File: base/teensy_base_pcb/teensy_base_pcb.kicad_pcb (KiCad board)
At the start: 2 copper layers, 69.8 x 48.3 mm, 26 parts, among them Q1 PN2222A, U1 LM7805CT, U2 LD1117V33, U3 Teensy_3.2, U4 nRF24L01+

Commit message: PCB updates / clean up.
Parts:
- removed R3: 10K, Resistors_ThroughHole:Resistor_Horizontal_RM10mm
- removed R4: 270, Resistors_ThroughHole:Resistor_Horizontal_RM10mm
- added R1: 10K, Resistors_ThroughHole:Resistor_Horizontal_RM10mm, F.Cu at (213.9, 104.1)
- added R2: 270, Resistors_ThroughHole:Resistor_Horizontal_RM10mm, F.Cu at (176.5, 101.6)
- moved U4 7.71 mm to (211.8, 87.4), turned to 180 degrees
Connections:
- U3 pad 21: Net-(P_SERVO1-Pad1) -> NC
- U3 pad 3: NC -> Net-(P_SERVO1-Pad1)
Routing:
- net Net-(P_SERVO1-Pad1): track 53.4 -> 25.1 mm
- net GND: track 80.8 -> 70.0 mm, vias 3 -> 5
- net +3.3V: track 149.4 -> 140.3 mm
- net Net-(U3-Pad12): track 18.1 -> 9.06 mm
- net Net-(U3-Pad13): track 31.3 -> 27.9 mm
- net Net-(U3-Pad10): track 12.0 -> 14.8 mm
- net Net-(U3-Pad11): track 14.5 -> 12.9 mm, vias 2 -> 0
- net Net-(U3-Pad14): track 29.3 -> 30.4 mm
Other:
- board text added: "Teensy 3"
- board text added: "nRF24L01"

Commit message: More PCB clean up / labels.
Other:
- board text added: "Cat Trainer rev. 1a"
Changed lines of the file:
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@@
     (area 158.674999 81.204999 228.675001 129.615001)
     (thickness 1.6)
-    (drawings 18)
+    (drawings 20)
     (tracks 154)
     (zones 0)
@@
     (descr "Film Capacitor Length 4mm x Width 2.5mm, Pitch 2.5mm")
     (tags Capacitor)
-    (fp_text reference C4 (at 1.25 -2.5 270) (layer F.SilkS)
+    (fp_text reference C4 (at 1.27 2.54 270) (layer F.SilkS)
       (effects (font (size 1 1) (thickness 0.15)))
     )
@@
     (descr "Film Capacitor Length 4mm x Width 2.5mm, Pitch 2.5mm")
     (tags Capacitor)
-    (fp_text reference C2 (at 1.27 -2.54 270) (layer F.SilkS)
+    (fp_text reference C2 (at 1.27 2.54 270) (layer F.SilkS)
       (effects (font (size 1 1) (thickness 0.15)))
     )
@@
     (descr "Radial Electrolytic Capacitor Diameter 10mm x Length 20mm, Pitch 5mm")
     (tags "Electrolytic Capacitor")
-    (fp_text reference C5 (at 1.27 -3.175) (layer F.SilkS)
+    (fp_text reference C5 (at 2.413 6.604) (layer F.SilkS)
       (effects (font (size 1 1) (thickness 0.15)))
     )
@@
     )
   )
+  (gr_text "Cat Trainer\nrev. 1a" (at 203.962 102.362 90) (layer B.SilkS)
+    (effects (font (size 2 2) (thickness 0.3)) (justify mirror))
+  )
+  (gr_text "Cat Trainer\nrev. 1a" (at 203.962 102.362 90) (layer F.SilkS)
+    (effects (font (size 2 2) (thickness 0.3)))
+  )
   (gr_line (start 193.802 90.932) (end 182.118 90.932) (angle 90) (layer F.SilkS) (width 0.2))
   (gr_line (start 193.802 101.6) (end 193.802 90.932) (angle 90) (layer F.SilkS) (width 0.2))
   (gr_line (start 182.118 101.6) (end 193.802 101.6) (angle 90) (layer F.SilkS) (width 0.2))
   (gr_line (start 182.118 90.932) (end 182.118 101.6) (angle 90) (layer F.SilkS) (width 0.2))
-  (gr_text nRF24L01 (at 208.28 99.695 90) (layer F.SilkS)
-    (effects (font (size 1.5 1.5) (thickness 0.2)))
+  (gr_text nRF24L01 (at 208.026 82.55) (layer F.SilkS)
+    (effects (font (size 1 1) (thickness 0.2)))
   )
   (gr_text "Teensy 3" (at 183.388 108.458 90) (layer F.SilkS)
@@
   (segment (start 180.34 99.06) (end 190.5 109.22) (width 0.1524) (layer F.Cu) (net 12))
   (segment (start 190.5 109.22) (end 190.5 118.11) (width 0.1524) (layer F.Cu) (net 12))
-  (segment (start 195.58 106.68) (end 197.358 106.68) (width 0.1524) (layer F.Cu) (net 13) (status 400000))
-  (segment (start 214.122 116.332) (end 215.9 118.11) (width 0.1524) (layer F.Cu) (net 13) (status 800000))
+  (segment (start 195.58 106.68) (end 197.358 106.68) (width 0.1524) (layer F.Cu) (net 13))
+  (segment (start 214.122 116.332) (end 215.9 118.11) (width 0.1524) (layer F.Cu) (net 13))
   (segment (start 207.01 116.332) (end 214.122 116.332) (width 0.1524) (layer F.Cu) (net 13))
   (segment (start 197.358 106.68) (end 207.01 116.332) (width 0.1524) (layer F.Cu) (net 13))
-  (segment (start 187.96 118.11) (end 187.96 124.46) (width 0.6096) (layer F.Cu) (net 14) (status 400000))
+  (segment (start 187.96 118.11) (end 187.96 124.46) (width 0.6096) (layer F.Cu) (net 14))
   (via (at 187.96 124.46) (size 0.6858) (drill 0.3302) (layers F.Cu B.Cu) (net 14))
-  (segment (start 195.58 116.84) (end 195.58 124.46) (width 0.6096) (layer F.Cu) (net 14) (status 400000))
+  (segment (start 195.58 116.84) (end 195.58 124.46) (width 0.6096) (layer F.Cu) (net 14))
   (via (at 195.58 124.46) (size 0.6858) (drill 0.3302) (layers F.Cu B.Cu) (net 14))
   (segment (start 169.5704 120.269) (end 169.5704 118.56974) (width 0.6096) (layer F.Cu) (net 14))

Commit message: Add accessory / future expansion ports to PCB.
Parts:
- added P_ACC1: CONN_01X03, Pin_Headers:Pin_Header_Straight_1x03, B.Cu at (211.6, 111.8)
- added P_ACC2: CONN_01X02, Pin_Headers:Pin_Header_Straight_1x02, B.Cu at (206.5, 94.0)
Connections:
- U3 pad 16: NC -> ACC2
- U3 pad 9: NC -> ACC1
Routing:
- net ACC2: track 0.00 -> 27.4 mm
- net ACC1: track 0.00 -> 14.5 mm
- net +3.3V: track 140.3 -> 152.7 mm
- net GND: track 70.0 -> 65.7 mm
- net +5V: track 103.7 -> 105.6 mm
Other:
- board text added: "3.3V"
- board text added: "5V"
- board text added: "A2"
- board text added: "D9"
- board text added: "GND"

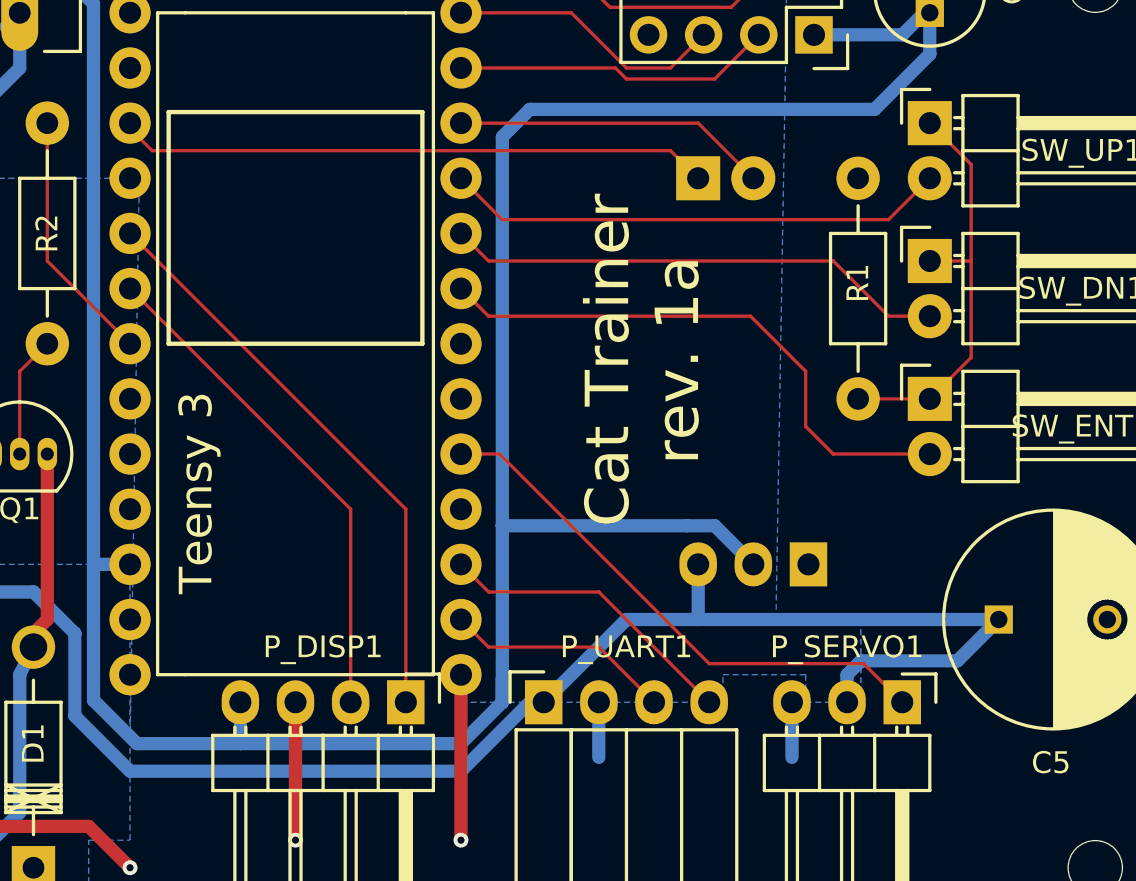
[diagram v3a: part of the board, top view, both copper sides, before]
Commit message: Reverse PCB Acc 3.3 / 5V pins and clean up traces.
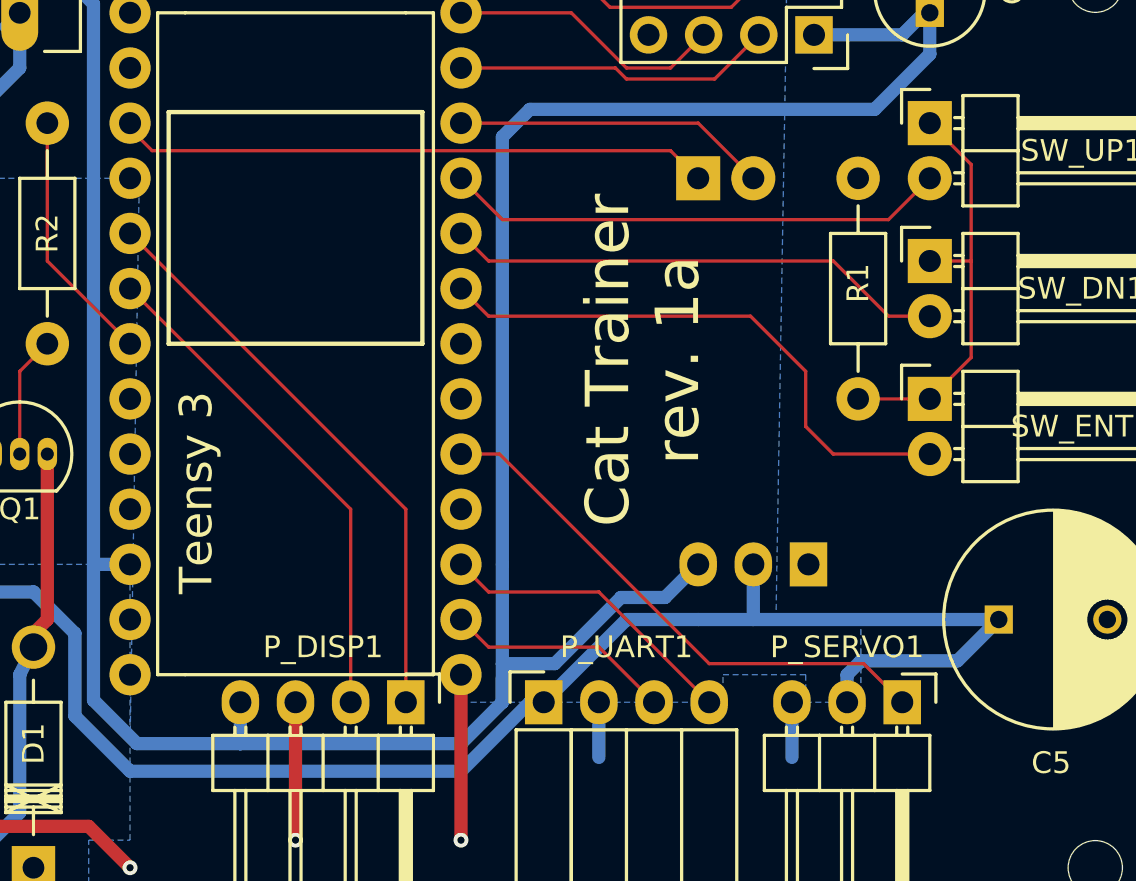
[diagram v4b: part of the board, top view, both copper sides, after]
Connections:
- P_ACC1 pad 2: +3.3V -> +5V
- P_ACC1 pad 3: +5V -> +3.3V
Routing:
- net +3.3V: track 152.7 -> 151.3 mm
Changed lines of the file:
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@@
     (thickness 1.6)
     (drawings 25)
-    (tracks 162)
+    (tracks 163)
     (zones 0)
     (modules 28)
@@
       (net 14 GND))
     (pad 2 thru_hole oval (at 0 -2.54 90) (size 2.032 1.7272) (drill 1.016) (layers *.Cu *.Mask B.SilkS)
+      (net 16 +5V))
+    (pad 3 thru_hole oval (at 0 -5.08 90) (size 2.032 1.7272) (drill 1.016) (layers *.Cu *.Mask B.SilkS)
       (net 17 +3.3V))
-    (pad 3 thru_hole oval (at 0 -5.08 90) (size 2.032 1.7272) (drill 1.016) (layers *.Cu *.Mask B.SilkS)
-      (net 16 +5V))
     (model Pin_Headers.3dshapes/Pin_Header_Straight_1x03.wrl
       (at (xyz 0 -0.1 0))
@@
     (effects (font (size 0.635 0.635) (thickness 0.127)) (justify mirror))
   )
-  (gr_text 5V (at 206.502 114.3 90) (layer B.SilkS)
+  (gr_text 3.3V (at 206.502 114.554 90) (layer B.SilkS)
     (effects (font (size 0.635 0.635) (thickness 0.127)) (justify mirror))
   )
-  (gr_text 3.3V (at 209.042 114.554 90) (layer B.SilkS)
+  (gr_text 5V (at 209.042 114.3 90) (layer B.SilkS)
     (effects (font (size 0.635 0.635) (thickness 0.127)) (justify mirror))
   )
@@
   (segment (start 168.91 111.90986) (end 168.91 104.14) (width 0.6096) (layer B.Cu) (net 15) (status 20))
   (segment (start 163.83 104.14) (end 168.91 104.14) (width 0.6096) (layer B.Cu) (net 15) (status 30))
-  (segment (start 206.502 111.76) (end 206.502 114.3) (width 0.6096) (layer B.Cu) (net 16) (status 400000))
+  (segment (start 209.042 111.76) (end 209.042 114.3) (width 0.6096) (layer B.Cu) (net 16))
   (segment (start 199.39 118.11) (end 198.755 118.11) (width 0.6096) (layer B.Cu) (net 16) (status 30))
   (segment (start 198.755 118.11) (end 195.58 121.285) (width 0.6096) (layer B.Cu) (net 16) (status 10))
   (segment (start 199.39 118.11) (end 203.2 114.3) (width 0.6096) (layer B.Cu) (net 16) (status 10))
-  (segment (start 203.2 114.3) (end 206.502 114.3) (width 0.6096) (layer B.Cu) (net 16) (status 20))
-  (segment (start 206.502 114.3) (end 220.345 114.3) (width 0.6096) (layer B.Cu) (net 16) (status 20))
+  (segment (start 206.502 114.3) (end 209.042 114.3) (width 0.6096) (layer B.Cu) (net 16) (status 20))
+  (segment (start 209.042 114.3) (end 220.345 114.3) (width 0.6096) (layer B.Cu) (net 16) (status 20))
   (segment (start 220.345 114.3) (end 218.44 116.205) (width 0.6096) (layer B.Cu) (net 16) (status 10))
   (segment (start 213.36 116.84) (end 213.36 118.11) (width 0.6096) (layer B.Cu) (net 16) (status 20))
@@
   (segment (start 175.26 88.9) (end 172.72 91.44) (width 0.6096) (layer B.Cu) (net 16) (status 20))
   (segment (start 174.625 86.995) (end 175.26 86.36) (width 0.6096) (layer B.Cu) (net 16) (status 30))
-  (segment (start 197.485 109.982) (end 205.994 109.982) (width 0.6096) (layer B.Cu) (net 17))
-  (segment (start 205.994 109.982) (end 207.264 109.982) (width 0.6096) (layer B.Cu) (net 17))
-  (segment (start 207.264 109.982) (end 209.042 111.76) (width 0.6096) (layer B.Cu) (net 17) (status 800000))
-  (segment (start 197.485 109.982) (end 197.612 109.982) (width 0.6096) (layer B.Cu) (net 17))
-  (segment (start 197.612 109.982) (end 197.485 109.982) (width 0.6096) (layer B.Cu) (net 17))
-  (segment (start 197.485 118.11) (end 197.485 117.094) (width 0.6096) (layer B.Cu) (net 17))
-  (segment (start 197.485 117.094) (end 197.485 116.967) (width 0.6096) (layer B.Cu) (net 17))
+  (segment (start 203.2 114.3) (end 206.502 114.3) (width 0.6096) (layer B.Cu) (net 16))
+  (segment (start 197.485 116.332) (end 199.898 116.332) (width 0.6096) (layer B.Cu) (net 17))
+  (segment (start 204.978 113.284) (end 206.502 111.76) (width 0.6096) (layer B.Cu) (net 17) (status 800000))
+  (segment (start 202.946 113.284) (end 204.978 113.284) (width 0.6096) (layer B.Cu) (net 17))
+  (segment (start 199.898 116.332) (end 202.946 113.284) (width 0.6096) (layer B.Cu) (net 17))
+  (segment (start 185.42 118.11) (end 185.42 120.015) (width 0.6096) (layer B.Cu) (net 17))
+  (segment (start 185.42 120.015) (end 185.42 119.888) (width 0.6096) (layer B.Cu) (net 17))
+  (segment (start 185.42 119.888) (end 185.42 120.015) (width 0.6096) (layer B.Cu) (net 17))
+  (segment (start 180.34 111.76) (end 178.656317 111.76) (width 0.6096) (layer B.Cu) (net 17))
+  (segment (start 197.485 118.11) (end 197.485 116.967) (width 0.6096) (layer B.Cu) (net 17))
+  (segment (start 197.485 92.075) (end 198.755 90.805) (width 0.6096) (layer B.Cu) (net 17))
+  (segment (start 198.755 90.805) (end 214.63 90.805) (width 0.6096) (layer B.Cu) (net 17))
+  (segment (start 197.485 118.11) (end 197.485 116.332) (width 0.6096) (layer B.Cu) (net 17))
+  (segment (start 197.485 116.332) (end 197.485 111.76) (width 0.6096) (layer B.Cu) (net 17))
+  (segment (start 197.485 111.76) (end 197.485 92.075) (width 0.6096) (layer B.Cu) (net 17))
+  (segment (start 195.58 120.015) (end 185.42 120.015) (width 0.6096) (layer B.Cu) (net 17))
+  (segment (start 185.42 120.015) (end 180.655632 120.015) (width 0.6096) (layer B.Cu) (net 17))
+  (segment (start 195.58 120.015) (end 197.485 118.11) (width 0.6096) (layer B.Cu) (net 17))
+  (segment (start 178.656317 118.015685) (end 180.655632 120.015) (width 0.6096) (layer B.Cu) (net 17))
   (segment (start 217.17 86.36) (end 216.916 86.36) (width 0.6096) (layer B.Cu) (net 17) (status 30))
   (segment (start 216.916 86.36) (end 215.9 87.376) (width 0.6096) (layer B.Cu) (net 17) (status 10))
   (segment (start 215.9 87.376) (end 211.836 87.376) (width 0.6096) (layer B.Cu) (net 17) (status 20))
   (segment (start 217.17 86.36) (end 217.17 88.265) (width 0.6096) (layer B.Cu) (net 17) (status 10))
-  (segment (start 197.485 92.075) (end 198.755 90.805) (width 0.6096) (layer B.Cu) (net 17))
-  (segment (start 198.755 90.805) (end 214.63 90.805) (width 0.6096) (layer B.Cu) (net 17))
   (segment (start 214.63 90.805) (end 217.17 88.265) (width 0.6096) (layer B.Cu) (net 17))
-  (segment (start 197.485 118.11) (end 197.485 116.332) (width 0.6096) (layer B.Cu) (net 17))
-  (segment (start 197.485 116.332) (end 197.485 109.982) (width 0.6096) (layer B.Cu) (net 17))
-  (segment (start 197.485 109.982) (end 197.485 92.075) (width 0.6096) (layer B.Cu) (net 17))
-  (segment (start 195.58 120.015) (end 185.42 120.015) (width 0.6096) (layer B.Cu) (net 17))
-  (segment (start 195.58 120.015) (end 197.485 118.11) (width 0.6096) (layer B.Cu) (net 17))
-  (segment (start 185.42 120.015) (end 185.42 118.11) (width 0.6096) (layer B.Cu) (net 17) (status 20))
-  (segment (start 180.34 111.76) (end 178.656317 111.76) (width 0.6096) (layer B.Cu) (net 17) (status 10))
   (segment (start 167.64 91.44) (end 167.64 85.09) (width 0.6096) (layer B.Cu) (net 17) (status 10))
-  (segment (start 180.655632 120.015) (end 185.42 120.015) (width 0.6096) (layer B.Cu) (net 17))
   (segment (start 178.656317 111.76) (end 178.656317 118.015685) (width 0.6096) (layer B.Cu) (net 17))
-  (segment (start 178.656317 118.015685) (end 180.655632 120.015) (width 0.6096) (layer B.Cu) (net 17))
   (segment (start 178.656317 85.946317) (end 178.656317 111.76) (width 0.6096) (layer B.Cu) (net 17))
   (segment (start 175.895 83.185) (end 178.656317 85.946317) (width 0.6096) (layer B.Cu) (net 17))
@@
   (segment (start 197.485 95.885) (end 195.58 93.98) (width 0.1524) (layer F.Cu) (net 20) (status 20))
   (segment (start 215.265 95.885) (end 197.485 95.885) (width 0.1524) (layer F.Cu) (net 20))
-  (segment (start 217.17 104.14) (end 213.36 104.14) (width 0.1524) (layer F.Cu) (net 21) (status 10))
+  (segment (start 217.17 104.14) (end 213.36 104.14) (width 0.1524) (layer F.Cu) (net 21) (status 30))
   (segment (start 217.17 97.79) (end 219.075 97.79) (width 0.1524) (layer F.Cu) (net 21) (status 10))
   (segment (start 217.17 91.44) (end 219.075 93.345) (width 0.1524) (layer F.Cu) (net 21) (status 10))
@@
   (segment (start 176.53 97.79) (end 176.53 91.44) (width 0.1524) (layer F.Cu) (net 22) (status 20))
   (segment (start 180.34 101.6) (end 176.53 97.79) (width 0.1524) (layer F.Cu) (net 22) (status 10))
-  (segment (start 180.34 91.44) (end 180.34 91.694) (width 0.1524) (layer F.Cu) (net 23))
-  (segment (start 180.34 91.694) (end 181.356 92.71) (width 0.1524) (layer F.Cu) (net 23))
+  (segment (start 180.34 91.44) (end 180.34 91.694) (width 0.1524) (layer F.Cu) (net 23) (status 30))
+  (segment (start 180.34 91.694) (end 181.356 92.71) (width 0.1524) (layer F.Cu) (net 23) (status 10))
   (segment (start 181.356 92.71) (end 205.232 92.71) (width 0.1524) (layer F.Cu) (net 23))
-  (segment (start 205.232 92.71) (end 206.502 93.98) (width 0.1524) (layer F.Cu) (net 23))
-  (segment (start 195.58 91.44) (end 206.502 91.44) (width 0.1524) (layer F.Cu) (net 24))
-  (segment (start 206.502 91.44) (end 209.042 93.98) (width 0.1524) (layer F.Cu) (net 24))
+  (segment (start 205.232 92.71) (end 206.502 93.98) (width 0.1524) (layer F.Cu) (net 23) (status 20))
+  (segment (start 195.58 91.44) (end 206.502 91.44) (width 0.1524) (layer F.Cu) (net 24) (status 10))
+  (segment (start 206.502 91.44) (end 209.042 93.98) (width 0.1524) (layer F.Cu) (net 24) (status 20))
   (zone (net 14) (net_name GND) (layer B.Cu) (hatch edge 0.508)
     (connect_pads (clearance 0.508))
